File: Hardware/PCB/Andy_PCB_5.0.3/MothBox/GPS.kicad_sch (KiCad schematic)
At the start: 22 parts, among them J5 Conn_1.25mm, Q11 JMTV210P02A, U10 Days, U11 Hours3, U12 MODE, U13 Hours1, U14 Hours2, U15 PCA9555PW, U16 PCA9555PW, U17 DS18B20U, U18 LTR-303ALS-01, U8 GPs 5 pin PM2.54-1*5, U9 PCA9555PW

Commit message: version 5.0.3 completed changes, as per CHANGELOG
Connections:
- net Armed/Disarmed: now also U11.16, U15.13 (IO1_0); no longer U11.9, U15.20 (IO1_7)
- net Fri: now also U11.13, U15.16 (IO1_3); no longer U11.14, U15.15 (IO1_2)
- net Mon: now also U11.9, U15.20 (IO1_7); no longer U11.10, U15.19 (IO1_6)
- net Sat: now also U11.14, U15.15 (IO1_2); no longer U11.15, U15.14 (IO1_1)
- net Sun: now also U11.15, U15.14 (IO1_1); no longer U11.16, U15.13 (IO1_0)
- net Thur: now also U11.12, U15.17 (IO1_4); no longer U11.13, U15.16 (IO1_3)
- net Tue: now also U11.10, U15.19 (IO1_6); no longer U11.11, U15.18 (IO1_5)
- net Wed: now also U11.11, U15.18 (IO1_5); no longer U11.12, U15.17 (IO1_4)
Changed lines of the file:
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@@
 	(title_block
 		(title "MothBox")
-		(date "2025-10-02")
-		(rev "5.0.2")
+		(date "2025-11-05")
+		(rev "5.0.3")
 		(company "Digital Naturalism Laboritories")
 		(comment 1 "and Parkview")
@@
 	)
 	(label "Tue"
-		(at 99.06 36.83 180)
+		(at 99.06 34.29 180)
 		(effects
 			(font
@@
 	)
 	(label "Fri"
-		(at 73.66 139.7 0)
+		(at 73.66 142.24 0)
 		(effects
 			(font
@@
 	)
 	(label "Wed"
-		(at 73.66 144.78 0)
+		(at 73.66 147.32 0)
 		(effects
 			(font
@@
 	)
 	(label "Mon"
-		(at 99.06 34.29 180)
+		(at 99.06 31.75 180)
 		(effects
 			(font
@@
 	)
 	(label "Thur"
-		(at 73.66 142.24 0)
+		(at 73.66 144.78 0)
 		(effects
 			(font
@@
 	)
 	(label "Thur"
-		(at 99.06 41.91 180)
+		(at 99.06 39.37 180)
 		(effects
 			(font
@@
 	)
 	(label "Armed{slash}Disarmed"
-		(at 73.66 152.4 0)
+		(at 73.66 134.62 0)
 		(effects
 			(font
@@
 	)
 	(label "Wed"
-		(at 99.06 39.37 180)
+		(at 99.06 36.83 180)
 		(effects
 			(font
@@
 	)
 	(label "Tue"
-		(at 73.66 147.32 0)
+		(at 73.66 149.86 0)
 		(effects
 			(font
@@
 	)
 	(label "Sat"
-		(at 73.66 137.16 0)
+		(at 73.66 139.7 0)
 		(effects
 			(font
@@
 	)
 	(label "Mon"
-		(at 73.66 149.86 0)
+		(at 73.66 152.4 0)
 		(effects
 			(font
@@
 	)
 	(label "Sun"
-		(at 99.06 49.53 180)
+		(at 99.06 46.99 180)
 		(effects
 			(font
@@
 	)
 	(label "Armed{slash}Disarmed"
-		(at 99.06 31.75 180)
+		(at 99.06 49.53 180)
 		(effects
 			(font
@@
 	)
 	(label "Sat"
-		(at 99.06 46.99 180)
+		(at 99.06 44.45 180)
 		(effects
 			(font
@@
 	)
 	(label "Sun"
-		(at 73.66 134.62 0)
+		(at 73.66 137.16 0)
 		(effects
 			(font
@@
 	)
 	(label "Fri"
-		(at 99.06 44.45 180)
+		(at 99.06 41.91 180)
 		(effects
 			(font

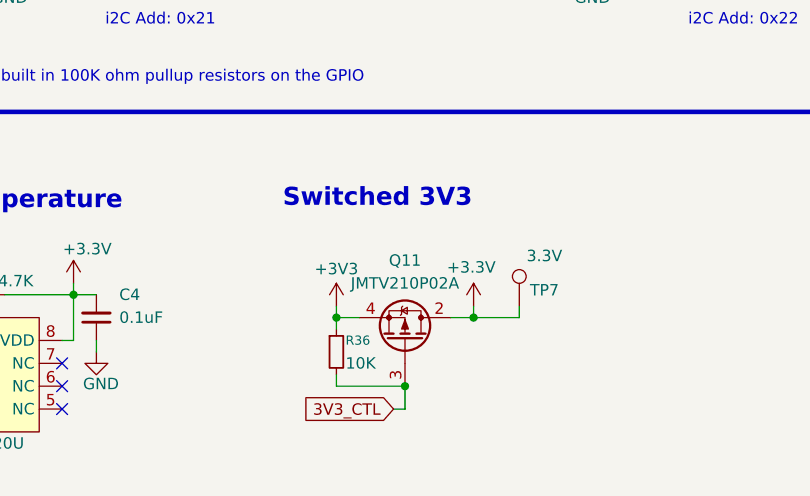
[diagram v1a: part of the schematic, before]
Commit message: swapped out Q1, Q8, Q10 for better specc'ed MOSFETs. Moved a few tracks around and updated CHANGELOG.txt
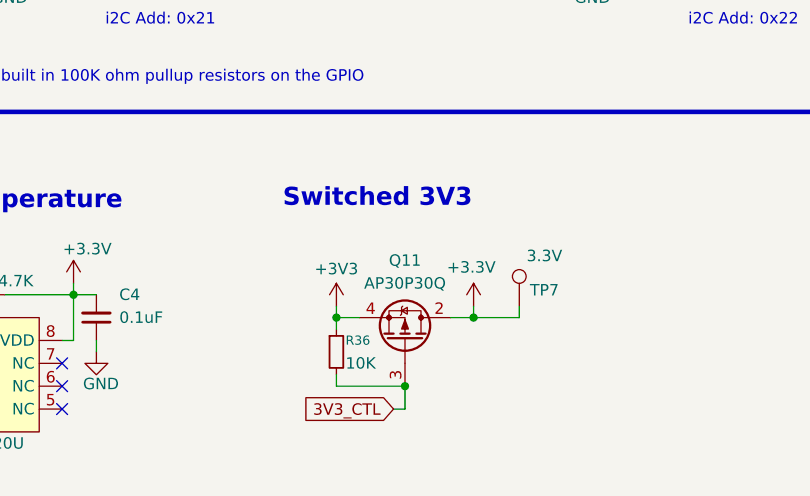
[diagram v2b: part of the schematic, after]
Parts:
- J5: symbol Connector:Conn_01x03_Pin -> MothBox_Symbol_Library:Conn_01x03_Pin
- Q11: value JMTV210P02A -> AP30P30Q; footprint MothBox_footprints_Library:U-DFN2020-6_L2.0-W2.0-P0.65-BL -> 0_easyeda_footprints:PDFN3333-8_L3.1-W3.2-P0.65-LS3.4-BL; LCSC_Part C2938482 -> C471913
- R33: LCSC_Part C25804 -> C23162
- U17: symbol 0_easyeda2kicad:DS18B20U -> MothBox_Symbol_Library:DS18B20U
- U18: symbol Sensor_Optical:LTR-303ALS-01 -> MothBox_Symbol_Library:LTR-303ALS-01
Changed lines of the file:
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@@
 	(title_block
 		(title "MothBox")
-		(date "2025-11-05")
+		(date "2025-11-14")
 		(rev "5.0.3")
 		(company "Digital Naturalism Laboritories")
@@
 	)
 	(symbol
-		(lib_id "power:+3V3")
+		(lib_id "MothBox_Symbol_Library:+3V3")
 		(at 152.4 190.5 0)
 		(unit 1)
@@
 	)
 	(symbol
-		(lib_id "Connector:Conn_01x03_Pin")
+		(lib_id "MothBox_Symbol_Library:Conn_01x03_Pin")
 		(at 274.32 160.02 0)
 		(mirror y)
@@
 			)
 		)
-		(property "LCSC_Part" "C25804"
+		(property "LCSC_Part" "C23162"
 			(at 113.03 189.23 0)
 			(effects
@@
 	)
 	(symbol
-		(lib_id "Sensor_Optical:LTR-303ALS-01")
+		(lib_id "MothBox_Symbol_Library:LTR-303ALS-01")
 		(at 55.88 194.31 0)
 		(unit 1)
@@
 	)
 	(symbol
-		(lib_id "0_easyeda2kicad:DS18B20U")
+		(lib_id "MothBox_Symbol_Library:DS18B20U")
 		(at 113.03 198.12 0)
 		(unit 1)
@@
 			)
 		)
-		(property "Value" "JMTV210P02A"
+		(property "Value" "AP30P30Q"
 			(at 160.02 187.96 90)
 			(effects
@@
 			)
 		)
-		(property "Footprint" "MothBox_footprints_Library:U-DFN2020-6_L2.0-W2.0-P0.65-BL"
+		(property "Footprint" "0_easyeda_footprints:PDFN3333-8_L3.1-W3.2-P0.65-LS3.4-BL"
 			(at 158.115 189.23 0)
 			(effects
@@
 			)
 		)
-		(property "LCSC_Part" "C2938482"
+		(property "LCSC_Part" "C471913"
 			(at 160.02 194.31 90)
 			(effects

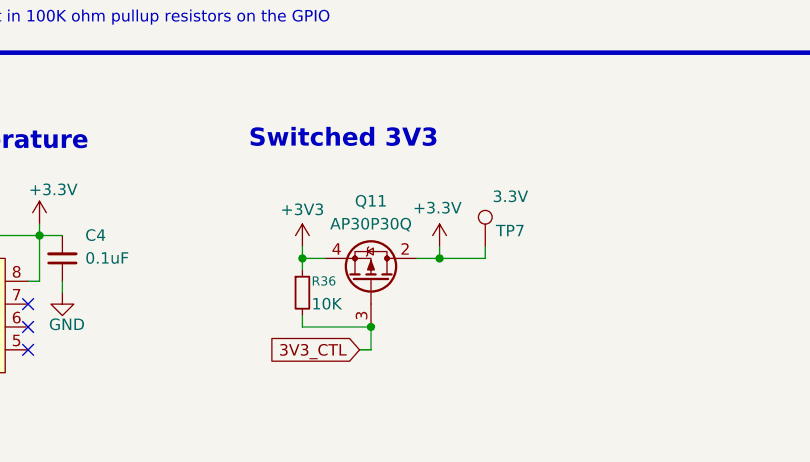
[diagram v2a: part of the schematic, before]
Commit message: Passes DRC - updated cuttable jumper, updated 3v3 mosfet, updated holes for battery
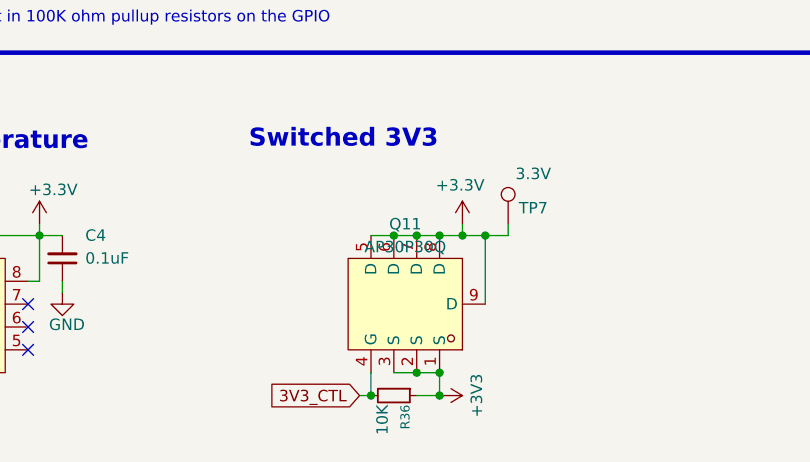
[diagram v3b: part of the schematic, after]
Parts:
- Q11: footprint 0_easyeda_footprints:PDFN3333-8_L3.1-W3.2-P0.65-LS3.4-BL -> easyeda2kicad:PDFN3333-8_L3.1-W3.2-P0.65-LS3.4-BL; symbol MothBox_Symbol_Library:JMTV210P02A -> easyeda2kicad:AP30P30Q; LCSC Part (none) -> C471913
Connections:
- net +3.3V: now also Q11.7 (D), Q11.9 (D); no longer Q11.1 (D), Q11.2 (D)
- net +3V3: now also Q11.1 (S), Q11.2 (S), Q11.3 (S); no longer Q11.4 (S), Q11.7 (S)
- net 3V3_CTL: now also Q11.4 (G); no longer Q11.3 (G)
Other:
- moved on the sheet: R36, TP7
